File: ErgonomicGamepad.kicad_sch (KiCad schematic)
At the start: 84 parts, among them J1 USB_C_Receptacle_USB2.0_16P, J2 Conn_01x08, J3 Conn_01x08, J4 Conn_01x08, J5 AVR-ISP-6, J6 Conn_01x08, J7 1824417, SW01 SW_DIP_x01, SW02 SW_DIP_x01, SW03 SW_DIP_x01, SW04 SW_DIP_x01, SW05 SW_DIP_x01, SW06 SW_DIP_x01, SW07 SW_DIP_x01, SW08 SW_DIP_x01, SW09 SW_DIP_x01, SW10 SW_DIP_x01, SW11 SW_DIP_x01, SW12 SW_DIP_x01, SW13 SW_DIP_x01, SW14 SW_DIP_x01, SW15 SW_DIP_x01, SW16 SW_DIP_x01, SW17 SW_DIP_x01, SW18 SW_DIP_x01, SW19 SW_DIP_x01, SW20 SW_DIP_x01, SW21 SW_DIP_x01, SW22 SW_DIP_x01, SW23 SW_DIP_x01, SW24 SW_DIP_x01, U1 ATmega32U4-A, U2 USBLC6-2SC6, Y1 Crystal

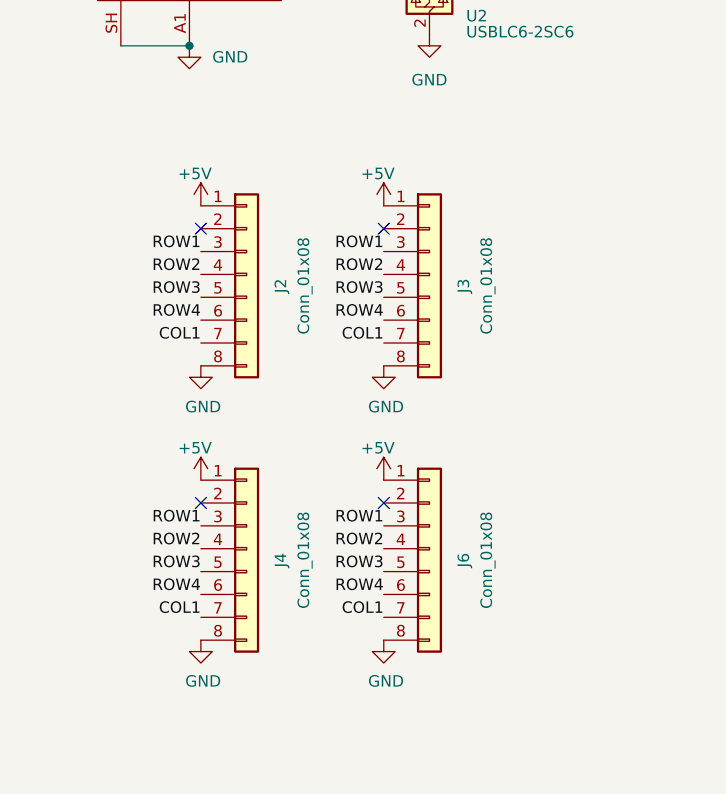
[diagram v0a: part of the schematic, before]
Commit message: Replace J2/J3/J4/J6 8-pin headers with 5-pin JST-XH, mark DNP
Satellite boards only need ROW1-4 + COL1 (matrix scanning needs no
local power), so drop the unused +5V/GND pin and two spares. Headers
are hand-soldered post-assembly, not JLCPCB-placed. Document vendor
sourcing for the JST-XH headers and F-F cables in the README.
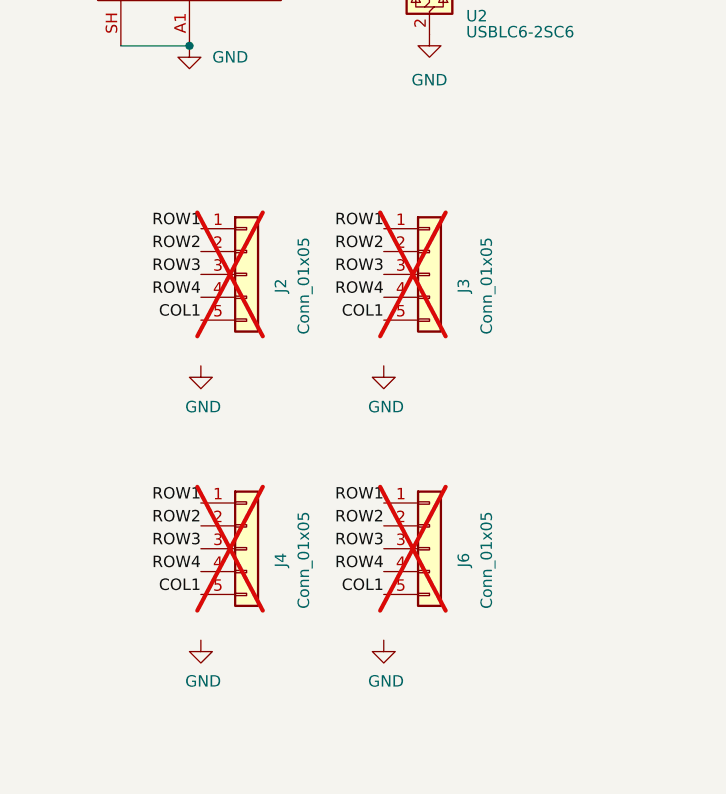
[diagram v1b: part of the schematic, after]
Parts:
- J2, J3, J4, J6: value Conn_01x08 -> Conn_01x05; footprint Connector_PinHeader_2.54mm:PinHeader_1x08_P2.54mm_Vertical -> Connector_JST:JST_XH_B5B-XH-A_1x05_P2.50mm_Vertical; symbol Connector_Generic:Conn_01x08 -> Connector_Generic:Conn_01x05; LCSC C124381 -> (none); MPN B-2100S08P-A110 -> (none); Manufacturer Ckmtw -> (none); Supplier LCSC -> (none); now not fitted
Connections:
- net +5V: no longer J2.1 (Pin_1), J3.1 (Pin_1), J4.1 (Pin_1), J6.1 (Pin_1)
- net COL1: now also J2.5 (Pin_5), J3.5 (Pin_5), J4.5 (Pin_5), J6.5 (Pin_5); no longer J2.7 (Pin_7), J3.7 (Pin_7), J4.7 (Pin_7), J6.7 (Pin_7)
- net GND: no longer J2.8 (Pin_8), J3.8 (Pin_8), J4.8 (Pin_8), J6.8 (Pin_8)
- net ROW1: now also J2.1 (Pin_1), J3.1 (Pin_1), J4.1 (Pin_1), J6.1 (Pin_1); no longer J2.3 (Pin_3), J3.3 (Pin_3), J4.3 (Pin_3), J6.3 (Pin_3)
- net ROW2: now also J2.2 (Pin_2), J3.2 (Pin_2), J4.2 (Pin_2), J6.2 (Pin_2); no longer J2.4 (Pin_4), J3.4 (Pin_4), J4.4 (Pin_4), J6.4 (Pin_4)
- net ROW3: now also J2.3 (Pin_3), J3.3 (Pin_3), J4.3 (Pin_3), J6.3 (Pin_3); no longer J2.5 (Pin_5), J3.5 (Pin_5), J4.5 (Pin_5), J6.5 (Pin_5)
- net ROW4: now also J2.4 (Pin_4), J3.4 (Pin_4), J4.4 (Pin_4), J6.4 (Pin_4); no longer J2.6 (Pin_6), J3.6 (Pin_6), J4.6 (Pin_6), J6.6 (Pin_6)
- no-connect marks 17 -> 13
